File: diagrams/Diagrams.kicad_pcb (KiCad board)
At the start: 2 copper layers, 9 parts

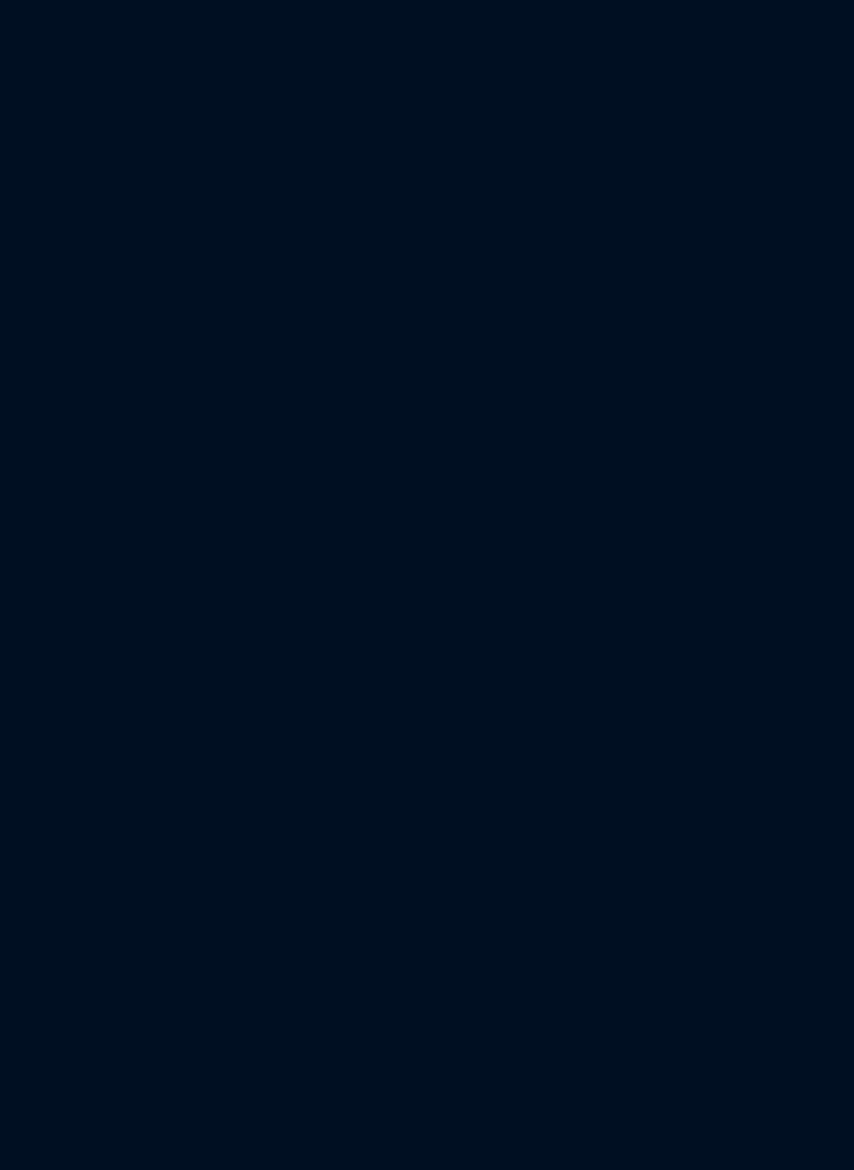
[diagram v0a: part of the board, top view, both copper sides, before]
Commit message: update: atribuição de footprints básicas na schematic
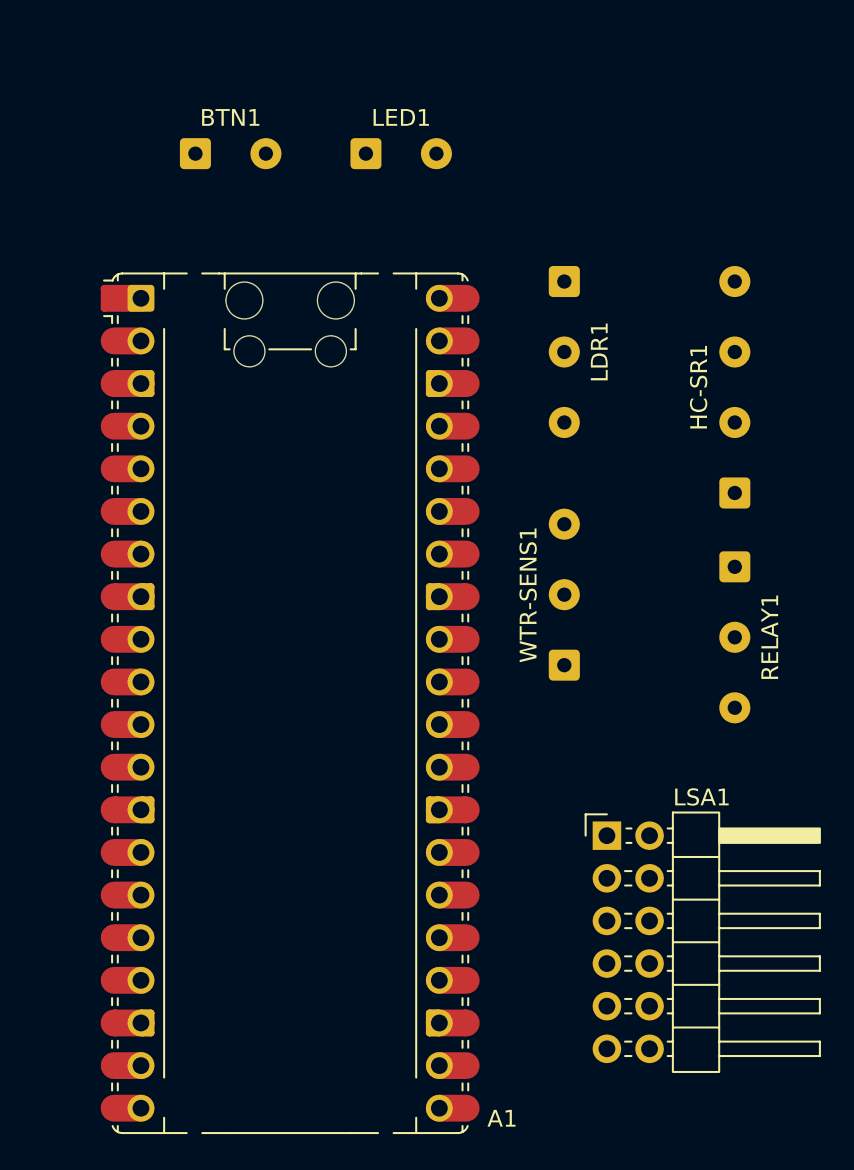
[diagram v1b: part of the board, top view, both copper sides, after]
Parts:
- added A1: RaspberryPi_Pico, Module:RaspberryPi_Pico_Common_Unspecified, F.Cu at (199.6, 121.7)
- added BTN1: BUTTON, Connector_Wire:SolderWire-0.25sqmm_1x02_P4.2mm_D0.65mm_OD1.7mm, F.Cu at (193.9, 88.9)
- added HC-SR1: HC-SR04, Connector_Wire:SolderWire-0.25sqmm_1x04_P4.2mm_D0.65mm_OD1.7mm, F.Cu at (226.1, 109.1)
- added LDR1: LDR, Connector_Wire:SolderWire-0.25sqmm_1x03_P4.2mm_D0.65mm_OD1.7mm, F.Cu at (215.9, 96.5)
- added LED1: LED, Connector_Wire:SolderWire-0.25sqmm_1x02_P4.2mm_D0.65mm_OD1.7mm, F.Cu at (204.1, 88.9)
- added LSA1: LogicSignalAMP, Connector_PinHeader_2.54mm:PinHeader_2x06_P2.54mm_Horizontal, F.Cu at (218.4, 129.5)
- added RELAY1: RELAY, Connector_Wire:SolderWire-0.25sqmm_1x03_P4.2mm_D0.65mm_OD1.7mm, F.Cu at (226.1, 113.5)
- added WTR-SENS1: WATER-SENSOR, Connector_Wire:SolderWire-0.25sqmm_1x03_P4.2mm_D0.65mm_OD1.7mm, F.Cu at (215.9, 119.4)

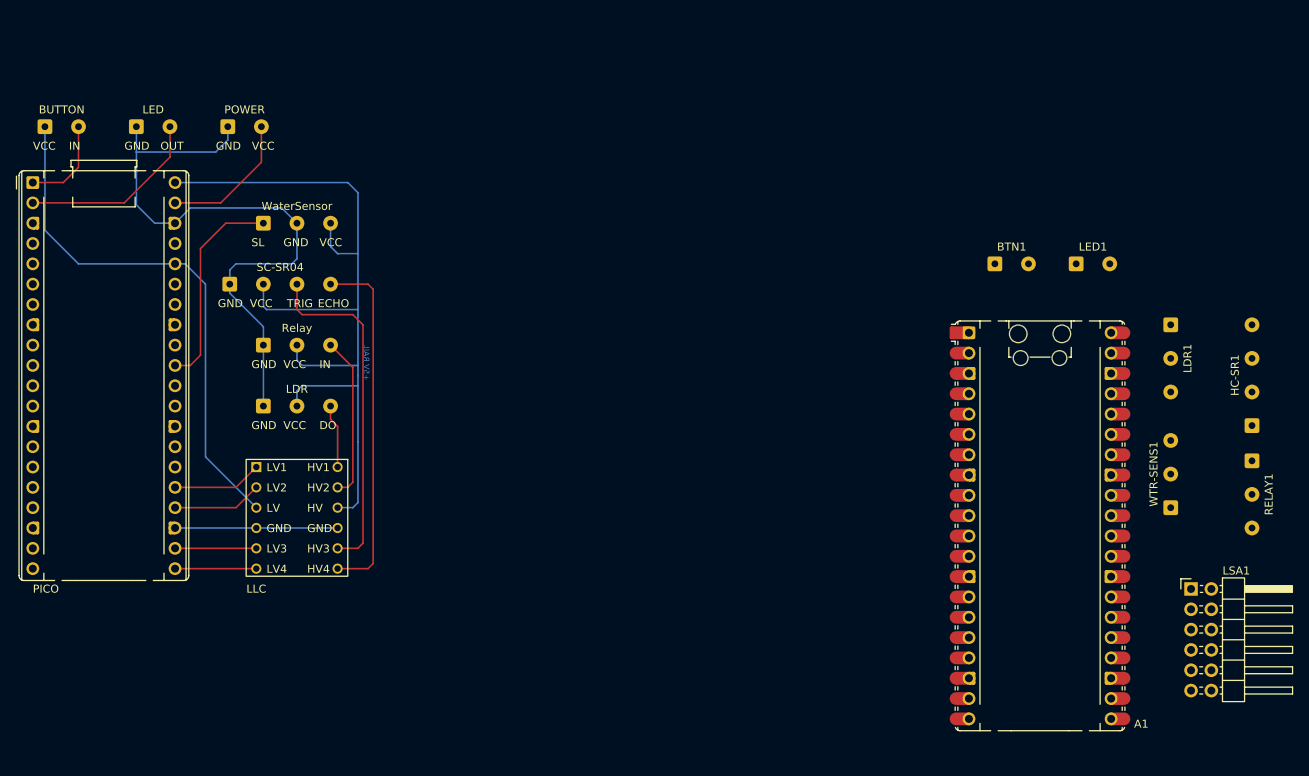
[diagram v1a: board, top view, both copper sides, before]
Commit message: feat(pcb): finalizar layout da PCB pronto para impressão
- concluir roteamento da placa
- ajustar posicionamento dos módulos
- corrigir outline da PCB em Edge.Cuts
- prontificar PCB para fabricação/impressão
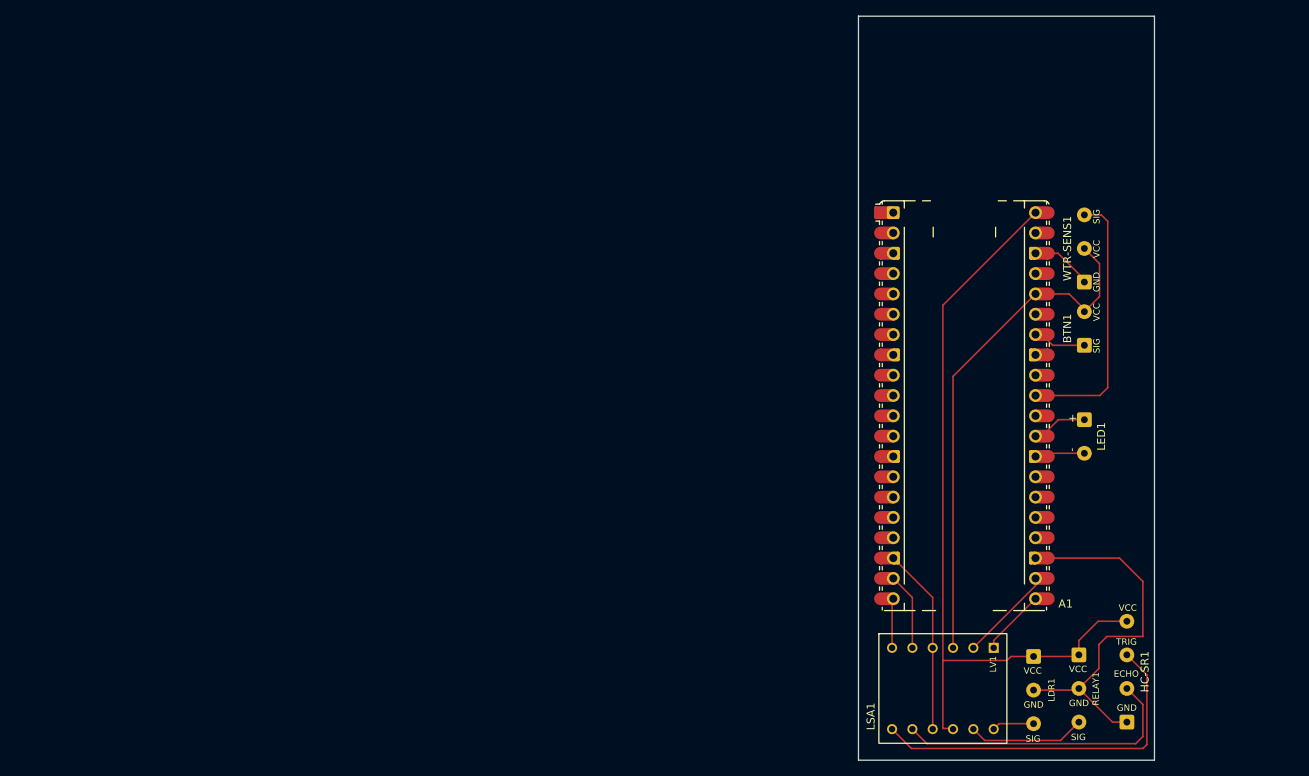
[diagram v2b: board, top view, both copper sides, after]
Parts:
- removed BUTTON, LED, POWER: SolderWire-0.25sqmm_1x02_P4.2mm_D0.65mm_OD1.7mm, Connector_Wire:SolderWire-0.25sqmm_1x02_P4.2mm_D0.65mm_OD1.7mm
- removed LDR, Relay, WaterSensor: SolderWire-0.25sqmm_1x03_P4.2mm_D0.65mm_OD1.7mm, Connector_Wire:SolderWire-0.25sqmm_1x03_P4.2mm_D0.65mm_OD1.7mm
- removed LLC: LLS-4C-Bd, een251:LLS-4C-Bd
- removed PICO: RaspberryPi_Pico_Common_THT, Module:RaspberryPi_Pico_Common_THT
- removed SC-SR04: SolderWire-0.25sqmm_1x04_P4.2mm_D0.65mm_OD1.7mm, Connector_Wire:SolderWire-0.25sqmm_1x04_P4.2mm_D0.65mm_OD1.7mm
- A1: footprint Module:RaspberryPi_Pico_Common_Unspecified -> Footprint-EEN251:RaspberryPi_Pico_Common_Unspecified
- LSA1: value LogicSignalAMP -> LLShifter; footprint Connector_PinHeader_2.54mm:PinHeader_2x06_P2.54mm_Horizontal -> Footprint-EEN251:LLShifer-Footprint
- moved LDR1 44.9 mm to (198.8, 138.0)
- moved HC-SR1 40.2 mm to (210.4, 146.2)
- moved LSA1 33.4 mm to (187.4, 142.0)
- moved RELAY1 32.5 mm to (204.4, 137.8)
- moved WTR-SENS1 30.2 mm to (205.1, 91.2)
- moved LED1 19.5 mm to (205.1, 108.4), turned to -90 degrees
- moved A1 17.7 mm to (190.1, 106.6)
- moved BTN1 15.1 mm to (205.1, 99.1), turned to 90 degrees
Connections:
- A1 pad 19: unconnected-(A1-GPIO14-Pad19) -> /GPIO14
- A1 pad 20: unconnected-(A1-GPIO15-Pad20) -> /GPIO15
- A1 pad 29: unconnected-(A1-GPIO22-Pad29) -> /GPIO22
- A1 pad 32: unconnected-(A1-GPIO27_ADC1-Pad32) -> /GPIO27
- A1 pad 34: unconnected-(A1-GPIO28_ADC2-Pad34) -> /GPIO28
- BTN1 pad 1: /GPIO0 -> /GPIO28
- LED1 pad 1: /GPIO1 -> /GPIO22
- LSA1 pad 1: /HV4 -> /GPIO16
- LSA1 pad 11: /GPIO17 -> /HV3
- LSA1 pad 12: /GPIO16 -> /HV4
- LSA1 pad 2: /HV3 -> /GPIO17
- LSA1 pad 3: GND -> +3V3
- LSA1 pad 4: +5V -> GND
- LSA1 pad 5: /HV2 -> /GPIO14
- LSA1 pad 6: /HV1 -> /GPIO15
- LSA1 pad 7: /GPIO19 -> /HV1
- LSA1 pad 8: /GPIO18 -> /HV2
- LSA1 pad 9: +3V3 -> +5V
- WTR-SENS1 pad 2: +5V -> +3V3
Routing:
- net (no net): track 508.2 -> 0.00 mm
- net +5V: track 0.00 -> 97.8 mm
- net GND: track 0.00 -> 84.3 mm
- net +3V3: track 0.00 -> 64.5 mm
- net /HV4: track 0.00 -> 45.3 mm
- net /HV3: track 0.00 -> 36.8 mm
- net /ADC0: track 0.00 -> 32.4 mm
- net /HV2: track 0.00 -> 14.7 mm
- net /GPIO17: track 0.00 -> 11.9 mm
- net /GPIO14: track 0.00 -> 9.67 mm
- net /GPIO16: track 0.00 -> 8.31 mm
- net /GPIO15: track 0.00 -> 6.20 mm
- net /GPIO28: track 0.00 -> 6.18 mm
- net /GPIO22: track 0.00 -> 6.16 mm
- net /HV1: track 0.00 -> 4.93 mm
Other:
- board outline added: 37 x 93 mm
- board text removed: "+5V RAIL"
